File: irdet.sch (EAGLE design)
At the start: 66 parts, among them IC1 MEGA8-AI, IC2 78L05F, J1 PSH02-04WG, J2 PSH02-04WG, J3 PSH02-04WG, J4 PSH02-04WG, J5 22-05-7098-09, T1 BC847, T2 BC857, T3 BC847, T4 BC857, T5 BC847, T6 BC857, T7 BC847, T8 BC857, X1 MVE252-5-V, X2 MVE252-5-V

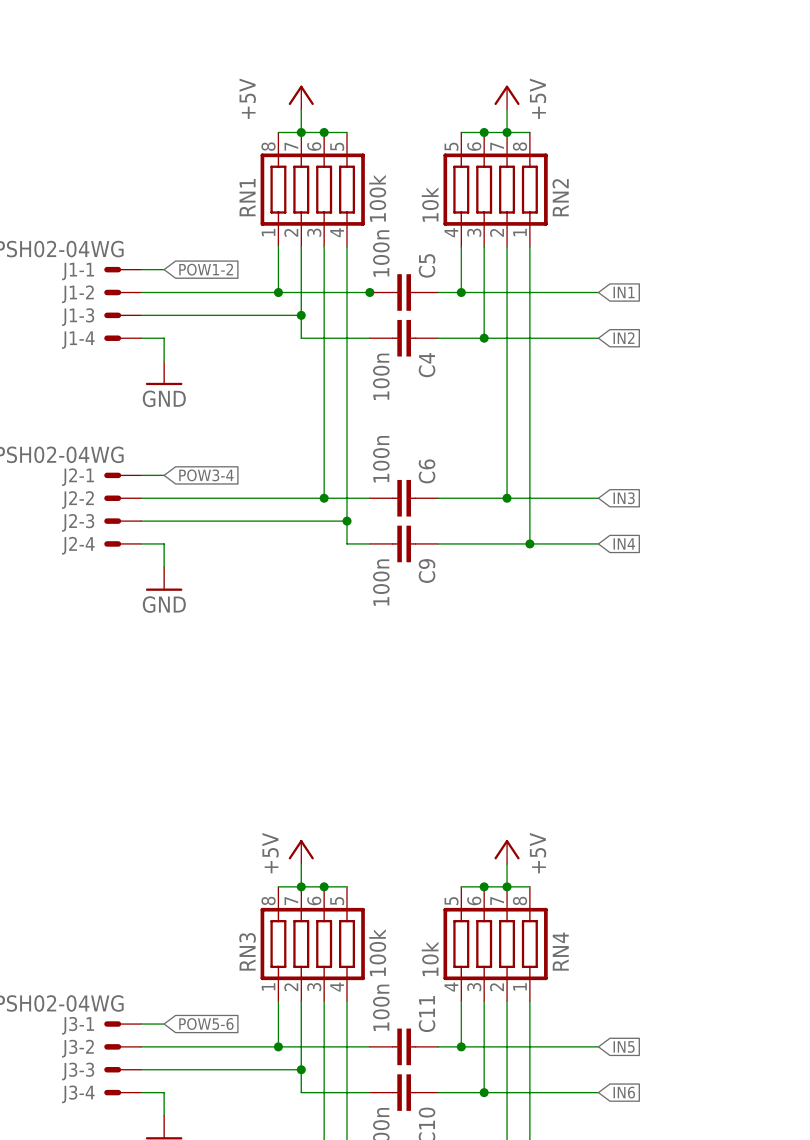
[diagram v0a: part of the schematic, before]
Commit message: Fix ERC issues.
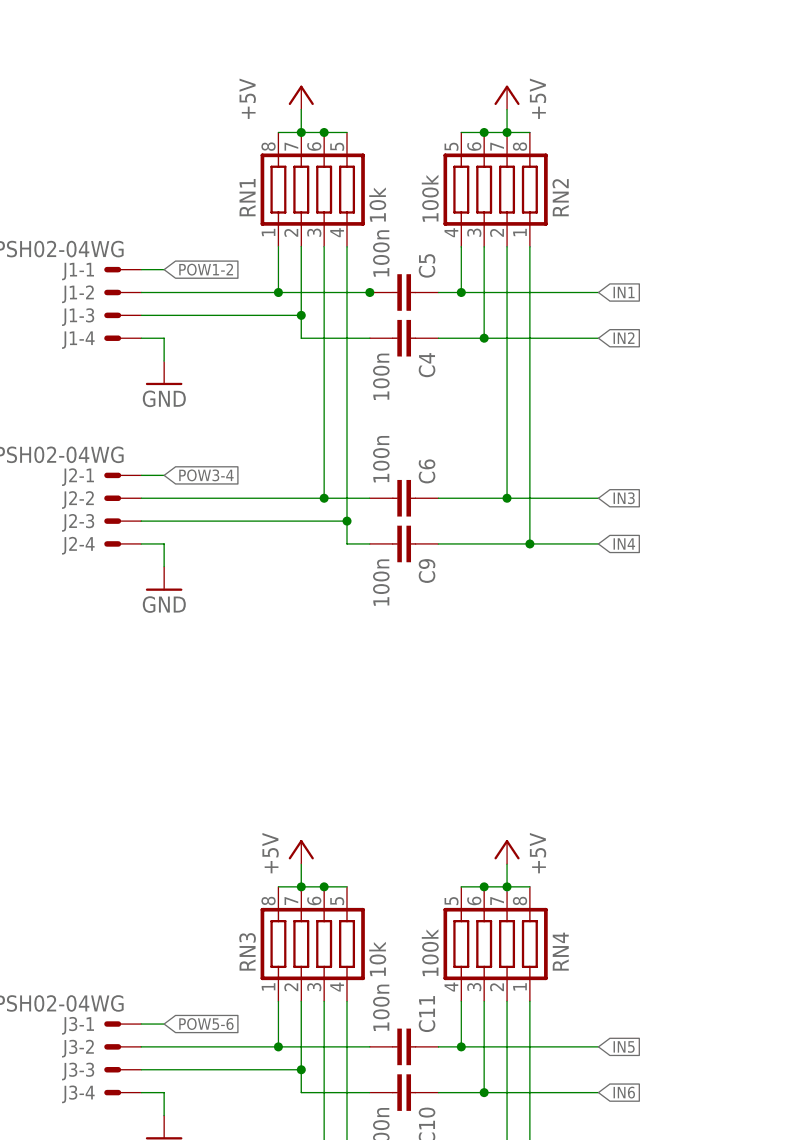
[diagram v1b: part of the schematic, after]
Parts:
- RN1, RN3: value 100k -> 10k; LCSC_PART C173315 -> C29718
- RN2, RN4: value 10k -> 100k; LCSC_PART C29718 -> C173315
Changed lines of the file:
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@@
 </part>
 <part name="GND3" library="supply1" library_urn="urn:adsk.eagle:library:371" deviceset="GND" device=""/>
-<part name="RN1" library="resistor-net" library_urn="urn:adsk.eagle:library:343" deviceset="CTS742C083" device="" package3d_urn="urn:adsk.eagle:package:24985/1" value="100k">
-<attribute name="LCSC_PART" value="C173315"/>
+<part name="RN1" library="resistor-net" library_urn="urn:adsk.eagle:library:343" deviceset="CTS742C083" device="" package3d_urn="urn:adsk.eagle:package:24985/1" value="10k">
+<attribute name="LCSC_PART" value="C29718"/>
 </part>
 <part name="C4" library="rcl" deviceset="C-EU" device="C0805" value="100n">
@@
 <attribute name="LCSC_PART" value="C49478"/>
 </part>
-<part name="RN2" library="resistor-net" library_urn="urn:adsk.eagle:library:343" deviceset="CTS742C083" device="" package3d_urn="urn:adsk.eagle:package:24985/1" value="10k">
-<attribute name="LCSC_PART" value="C29718"/>
+<part name="RN2" library="resistor-net" library_urn="urn:adsk.eagle:library:343" deviceset="CTS742C083" device="" package3d_urn="urn:adsk.eagle:package:24985/1" value="100k">
+<attribute name="LCSC_PART" value="C173315"/>
 </part>
 <part name="J2" library="con-molex" library_urn="urn:adsk.eagle:library:165" deviceset="22-?-04" device="05-7048" package3d_urn="urn:adsk.eagle:package:8078648/1" value="PSH02-04WG"/>
@@
 <part name="J3" library="con-molex" library_urn="urn:adsk.eagle:library:165" deviceset="22-?-04" device="05-7048" package3d_urn="urn:adsk.eagle:package:8078648/1" value="PSH02-04WG"/>
 <part name="GND5" library="supply1" library_urn="urn:adsk.eagle:library:371" deviceset="GND" device=""/>
-<part name="RN3" library="resistor-net" library_urn="urn:adsk.eagle:library:343" deviceset="CTS742C083" device="" package3d_urn="urn:adsk.eagle:package:24985/1" value="100k">
-<attribute name="LCSC_PART" value="C173315"/>
+<part name="RN3" library="resistor-net" library_urn="urn:adsk.eagle:library:343" deviceset="CTS742C083" device="" package3d_urn="urn:adsk.eagle:package:24985/1" value="10k">
+<attribute name="LCSC_PART" value="C29718"/>
 </part>
 <part name="C10" library="rcl" deviceset="C-EU" device="C0805" value="100n">
@@
 <attribute name="LCSC_PART" value="C49478"/>
 </part>
-<part name="RN4" library="resistor-net" library_urn="urn:adsk.eagle:library:343" deviceset="CTS742C083" device="" package3d_urn="urn:adsk.eagle:package:24985/1" value="10k">
-<attribute name="LCSC_PART" value="C29718"/>
+<part name="RN4" library="resistor-net" library_urn="urn:adsk.eagle:library:343" deviceset="CTS742C083" device="" package3d_urn="urn:adsk.eagle:package:24985/1" value="100k">
+<attribute name="LCSC_PART" value="C173315"/>
 </part>
 <part name="J4" library="con-molex" library_urn="urn:adsk.eagle:library:165" deviceset="22-?-04" device="05-7048" package3d_urn="urn:adsk.eagle:package:8078648/1" value="PSH02-04WG"/>

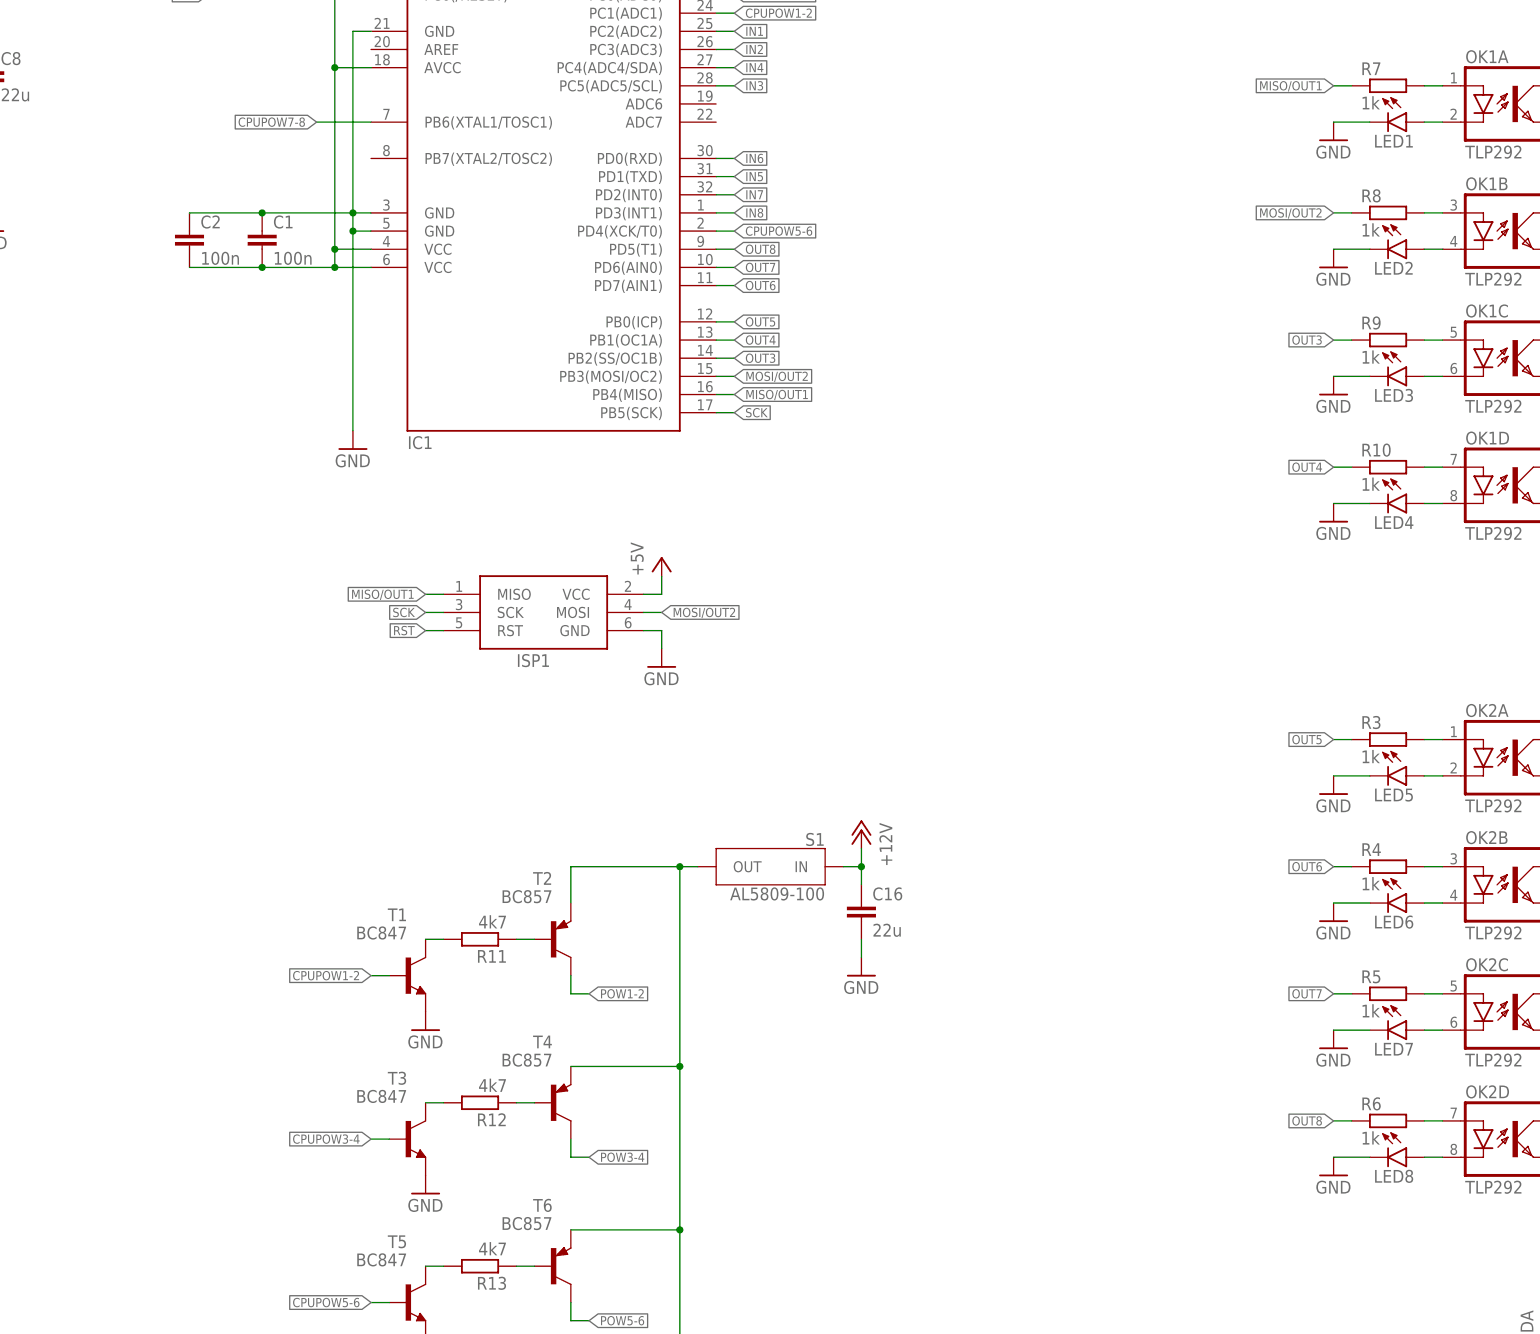
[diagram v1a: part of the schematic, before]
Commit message: Add status LED.
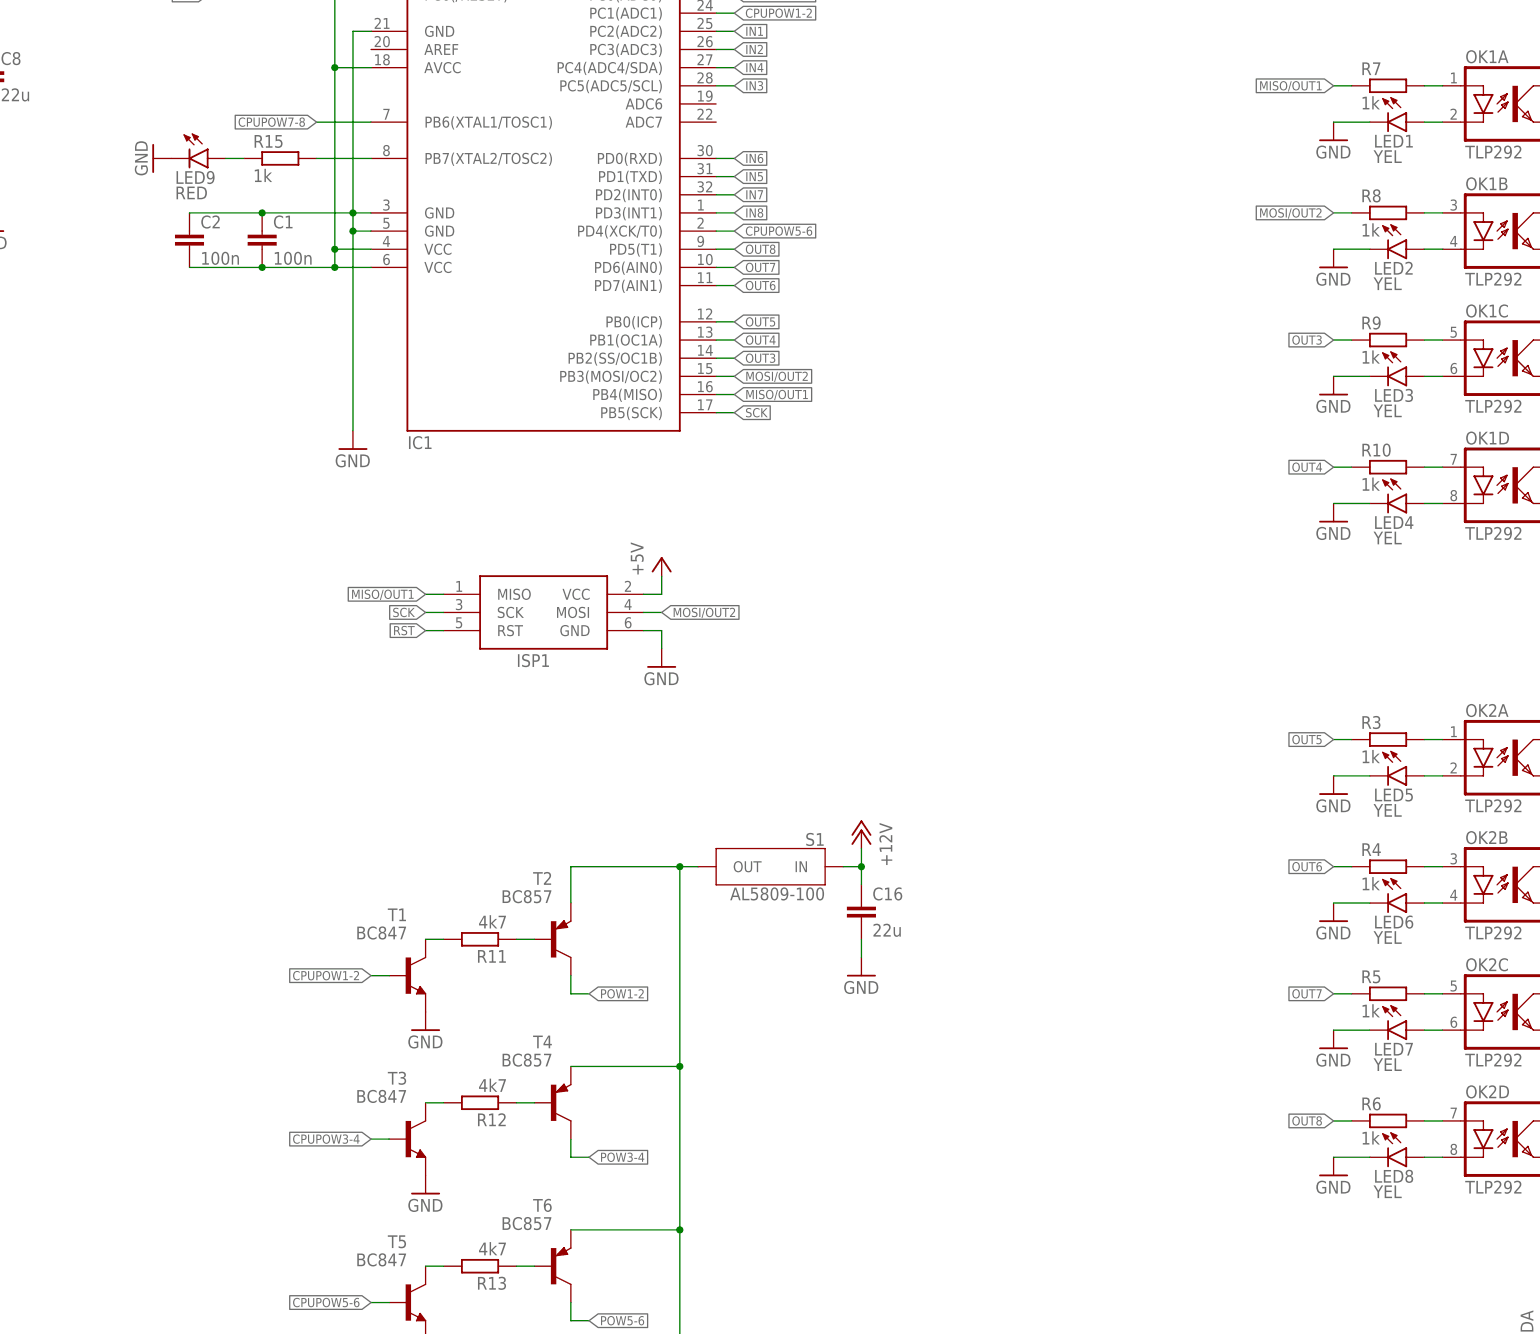
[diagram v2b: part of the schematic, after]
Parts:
- added LED9: RED, led:LEDCHIPLED_0805
- added R15: 1k, rcl:R-EU_R0805
- LED1, LED2, LED3, LED4, LED5, LED6, LED7, LED8: value (none) -> YEL
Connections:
- new net N$34: IC1.PB7(XTAL2/TOSC2), R15.2
- new net N$47: LED9.A, R15.1
- net GND: now also LED9.C
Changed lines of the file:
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@@
 <attribute name="LCSC_PART" value="C17513"/>
 </part>
-<part name="LED5" library="led" library_urn="urn:adsk.eagle:library:259" deviceset="LED" device="CHIPLED_0805" package3d_urn="urn:adsk.eagle:package:15821/2"/>
-<part name="LED6" library="led" library_urn="urn:adsk.eagle:library:259" deviceset="LED" device="CHIPLED_0805" package3d_urn="urn:adsk.eagle:package:15821/2"/>
-<part name="LED7" library="led" library_urn="urn:adsk.eagle:library:259" deviceset="LED" device="CHIPLED_0805" package3d_urn="urn:adsk.eagle:package:15821/2"/>
-<part name="LED8" library="led" library_urn="urn:adsk.eagle:library:259" deviceset="LED" device="CHIPLED_0805" package3d_urn="urn:adsk.eagle:package:15821/2"/>
+<part name="LED5" library="led" library_urn="urn:adsk.eagle:library:259" deviceset="LED" device="CHIPLED_0805" package3d_urn="urn:adsk.eagle:package:15821/2" value="YEL"/>
+<part name="LED6" library="led" library_urn="urn:adsk.eagle:library:259" deviceset="LED" device="CHIPLED_0805" package3d_urn="urn:adsk.eagle:package:15821/2" value="YEL"/>
+<part name="LED7" library="led" library_urn="urn:adsk.eagle:library:259" deviceset="LED" device="CHIPLED_0805" package3d_urn="urn:adsk.eagle:package:15821/2" value="YEL"/>
+<part name="LED8" library="led" library_urn="urn:adsk.eagle:library:259" deviceset="LED" device="CHIPLED_0805" package3d_urn="urn:adsk.eagle:package:15821/2" value="YEL"/>
 <part name="GND7" library="supply1" library_urn="urn:adsk.eagle:library:371" deviceset="GND" device=""/>
 <part name="GND8" library="supply1" library_urn="urn:adsk.eagle:library:371" deviceset="GND" device=""/>
@@
 <attribute name="LCSC_PART" value="C17513"/>
 </part>
-<part name="LED1" library="led" library_urn="urn:adsk.eagle:library:259" deviceset="LED" device="CHIPLED_0805" package3d_urn="urn:adsk.eagle:package:15821/2"/>
-<part name="LED2" library="led" library_urn="urn:adsk.eagle:library:259" deviceset="LED" device="CHIPLED_0805" package3d_urn="urn:adsk.eagle:package:15821/2"/>
-<part name="LED3" library="led" library_urn="urn:adsk.eagle:library:259" deviceset="LED" device="CHIPLED_0805" package3d_urn="urn:adsk.eagle:package:15821/2"/>
-<part name="LED4" library="led" library_urn="urn:adsk.eagle:library:259" deviceset="LED" device="CHIPLED_0805" package3d_urn="urn:adsk.eagle:package:15821/2"/>
+<part name="LED1" library="led" library_urn="urn:adsk.eagle:library:259" deviceset="LED" device="CHIPLED_0805" package3d_urn="urn:adsk.eagle:package:15821/2" value="YEL"/>
+<part name="LED2" library="led" library_urn="urn:adsk.eagle:library:259" deviceset="LED" device="CHIPLED_0805" package3d_urn="urn:adsk.eagle:package:15821/2" value="YEL"/>
+<part name="LED3" library="led" library_urn="urn:adsk.eagle:library:259" deviceset="LED" device="CHIPLED_0805" package3d_urn="urn:adsk.eagle:package:15821/2" value="YEL"/>
+<part name="LED4" library="led" library_urn="urn:adsk.eagle:library:259" deviceset="LED" device="CHIPLED_0805" package3d_urn="urn:adsk.eagle:package:15821/2" value="YEL"/>
 <part name="GND11" library="supply1" library_urn="urn:adsk.eagle:library:371" deviceset="GND" device=""/>
 <part name="GND12" library="supply1" library_urn="urn:adsk.eagle:library:371" deviceset="GND" device=""/>
@@
 <part name="GND30" library="supply1" library_urn="urn:adsk.eagle:library:371" deviceset="GND" device=""/>
 <part name="X2" library="con-malina" deviceset="MVE252-5-V" device=""/>
+<part name="LED9" library="led" library_urn="urn:adsk.eagle:library:259" deviceset="LED" device="CHIPLED_0805" package3d_urn="urn:adsk.eagle:package:15821/2" value="RED"/>
+<part name="R15" library="rcl" deviceset="R-EU_" device="R0805" value="1k">
+<attribute name="LCSC_PART" value="C17513"/>
+</part>
+<part name="GND31" library="supply1" library_urn="urn:adsk.eagle:library:371" deviceset="GND" device=""/>
 </parts>
 <sheets>
@@
 <instance part="X2" gate="-2" x="27.94" y="210.82" smashed="yes" rot="MR0">
 <attribute name="NAME" x="23.876" y="210.058" size="1.778" layer="95" rot="MR0"/>
+</instance>
+<instance part="LED9" gate="G$1" x="149.86" y="210.82" smashed="yes" rot="R270">
+<attribute name="NAME" x="145.288" y="207.264" size="1.778" layer="95"/>
+<attribute name="VALUE" x="145.288" y="205.105" size="1.778" layer="96"/>
+</instance>
+<instance part="R15" gate="G$1" x="160.02" y="210.82" smashed="yes">
+<attribute name="NAME" x="156.21" y="212.3186" size="1.778" layer="95"/>
+<attribute name="VALUE" x="156.21" y="207.518" size="1.778" layer="96"/>
+<attribute name="LCSC_PART" x="160.02" y="210.82" size="1.778" layer="96" display="off"/>
+</instance>
+<instance part="GND31" gate="1" x="142.24" y="210.82" smashed="yes" rot="R270">
+<attribute name="VALUE" x="139.7" y="213.36" size="1.778" layer="96" rot="R270"/>
 </instance>
 </instances>
@@
 <wire x1="241.3" y1="99.06" x2="241.3" y2="101.6" width="0.1524" layer="91"/>
 </segment>
+<segment>
+<pinref part="LED9" gate="G$1" pin="C"/>
+<pinref part="GND31" gate="1" pin="GND"/>
+</segment>
 </net>
 <net name="MISO/OUT1" class="0">
@@
 </segment>
 </net>
+<net name="N$34" class="0">
+<segment>
+<pinref part="R15" gate="G$1" pin="2"/>
+<pinref part="IC1" gate="G$1" pin="PB7(XTAL2/TOSC2)"/>
+<wire x1="165.1" y1="210.82" x2="172.72" y2="210.82" width="0.1524" layer="91"/>
+</segment>
+</net>
+<net name="N$47" class="0">
+<segment>
+<pinref part="LED9" gate="G$1" pin="A"/>
+<pinref part="R15" gate="G$1" pin="1"/>
+<wire x1="152.4" y1="210.82" x2="154.94" y2="210.82" width="0.1524" layer="91"/>
+</segment>
+</net>
 </nets>
 </sheet>
 </sheets>
+<errors>
+</errors>
 </schematic>
 </drawing>
